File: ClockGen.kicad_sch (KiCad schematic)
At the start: 27 parts, among them Q1 2N4258, Q2 2N4258, Y1 XT0001

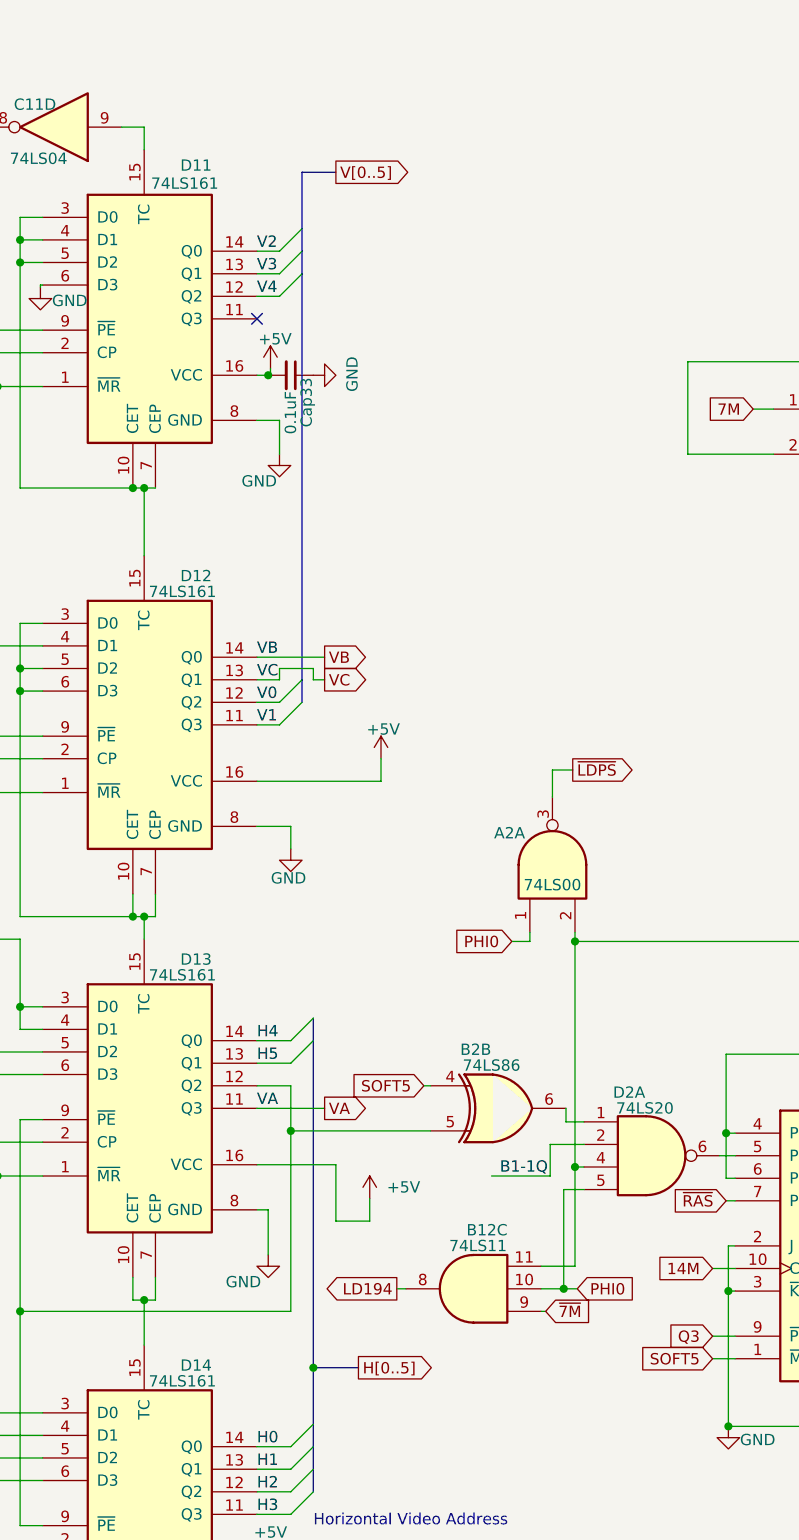
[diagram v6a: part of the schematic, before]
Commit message: add missing test points
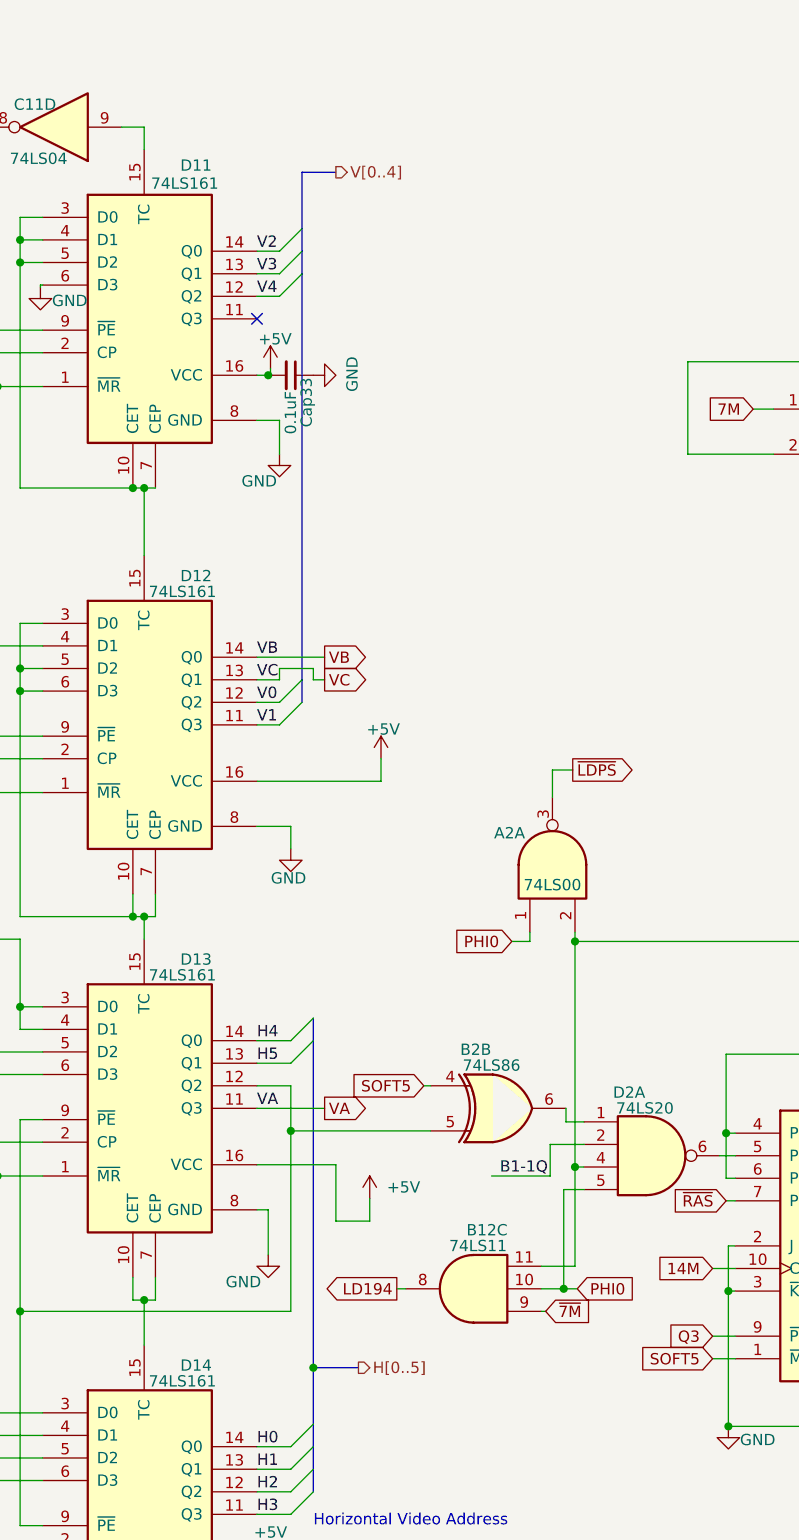
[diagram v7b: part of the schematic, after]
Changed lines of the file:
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@@
-    )
-  )
-  (global_label "H[0..5]" (shape output) (at 175.26 194.31 0)
-    (effects (font (size 1.27 1.27)) (justify left))
-    (property "Intersheetrefs" "${INTERSHEET_REFS}" (at 175.26 194.31 0)
-      (effects (font (size 1.27 1.27)) hide)
     )
   )
@@
     (effects (font (size 1.27 1.27)) (justify right))
     (property "Intersheetrefs" "${INTERSHEET_REFS}" (at 233.68 104.14 0)
-      (effects (font (size 1.27 1.27)) hide)
-    )
-  )
-  (global_label "V[0..5]" (shape output) (at 172.72 59.69 0)
-    (effects (font (size 1.27 1.27)) (justify left))
-    (property "Intersheetrefs" "${INTERSHEET_REFS}" (at 172.72 59.69 0)
       (effects (font (size 1.27 1.27)) hide)
     )
@@
     (effects (font (size 1.27 1.27)) (justify right))
   )
+  (hierarchical_label "H[0..5]" (shape output) (at 175.26 194.31 0) (fields_autoplaced)
+    (effects (font (size 1.27 1.27)) (justify left))
+  )
+  (hierarchical_label "V[0..4]" (shape output) (at 172.72 59.69 0) (fields_autoplaced)
+    (effects (font (size 1.27 1.27)) (justify left))
+  )
   (symbol (lib_id "AppleII+:74LS161") (at 152.4 77.47 0) (unit 1)
